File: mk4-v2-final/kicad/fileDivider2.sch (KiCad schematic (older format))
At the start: 2 parts

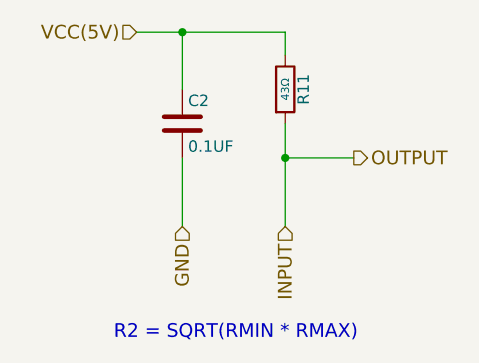
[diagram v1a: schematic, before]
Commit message: added headnight diodes, I don't think software control of them is going to be possible
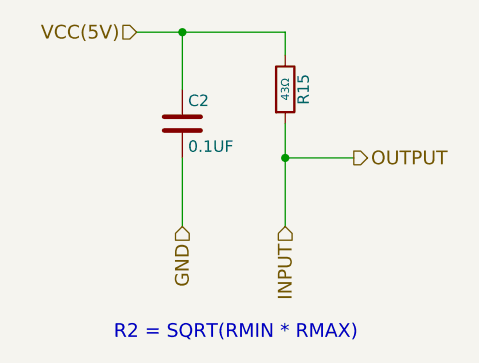
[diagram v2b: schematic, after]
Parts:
- renumbered R11 to R15
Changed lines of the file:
@@
 $EndDescr
 $Comp
-L R R11
+L R R15
 U 1 1 59DE51A6
 P 5850 3200
-F 0 "R11" V 5930 3200 50  0000 C CNN
+F 0 "R15" V 5930 3200 50  0000 C CNN
 F 1 "43Ω" V 5850 3200 35  0000 C CNN
 F 2 "Resistors_THT:R_Axial_DIN0207_L6.3mm_D2.5mm_P10.16mm_Horizontal" V 5780 3200 50  0001 C CNN

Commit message: schematic is done, footprint association and netlist are also done
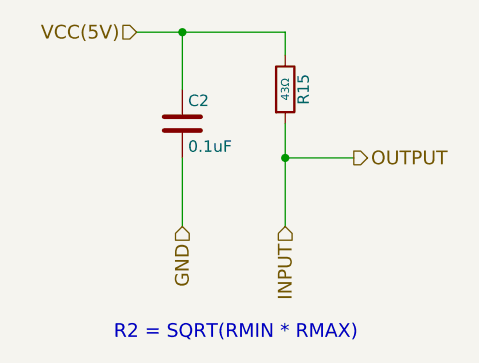
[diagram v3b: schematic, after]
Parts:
- C2: value 0.1UF -> 0.1uF; footprint Capacitors_THT:CP_Radial_D5.0mm_P2.00mm -> C_Rect_L5.08mm_W3.175mm_P2.54mm:C_Rect_L5.08mm_W3.175mm_P2.54mm; digikey-pn (none) -> 478-5096-ND; mfg-pn (none) -> AR205F104K4R
- R15: footprint Resistors_THT:R_Axial_DIN0207_L6.3mm_D2.5mm_P10.16mm_Horizontal -> Resistors_THT:R_Axial_DIN0204_L3.6mm_D1.6mm_P5.08mm_Horizontal; digikey-pn (none) -> BC4443CT-ND; mfg-pn (none) -> MBA02040C4309FC100
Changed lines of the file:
@@
 EESchema Schematic File Version 2
-LIBS:hitchco-mk4-rescue
 LIBS:power
 LIBS:device
@@
 LIBS:cd4013b
 LIBS:ncs3s1205sc
+LIBS:lca715
+LIBS:SN74HC595N
+LIBS:CD74HC4067
 LIBS:hitchco-mk4-cache
 EELAYER 25 0
@@
 F 0 "R15" V 5930 3200 50  0000 C CNN
 F 1 "43Ω" V 5850 3200 35  0000 C CNN
-F 2 "Resistors_THT:R_Axial_DIN0207_L6.3mm_D2.5mm_P10.16mm_Horizontal" V 5780 3200 50  0001 C CNN
+F 2 "Resistors_THT:R_Axial_DIN0204_L3.6mm_D1.6mm_P5.08mm_Horizontal" V 5780 3200 50  0001 C CNN
 F 3 "" H 5850 3200 50  0001 C CNN
+F 4 "BC4443CT-ND" H 5930 3300 50  0001 C CNN "digikey-pn"
+F 5 "MBA02040C4309FC100" H 5930 3300 50  0001 C CNN "mfg-pn"
 	1    5850 3200
+	1    0    0    -1
+$EndComp
+$Comp
+L C C2
+U 1 1 5A23F9FC
+P 5400 3350
+F 0 "C2" H 5425 3450 50  0000 L CNN
+F 1 "0.1uF" H 5425 3250 50  0000 L CNN
+F 2 "C_Rect_L5.08mm_W3.175mm_P2.54mm:C_Rect_L5.08mm_W3.175mm_P2.54mm" H 5438 3200 50  0001 C CNN
+F 3 "http://datasheets.avx.com/AR-Series.pdf" H 5400 3350 50  0001 C CNN
+F 4 "478-5096-ND" H 5425 3550 50  0001 C CNN "digikey-pn"
+F 5 "AR205F104K4R" H 5425 3550 50  0001 C CNN "mfg-pn"
+	1    5400 3350
 	1    0    0    -1
 $EndComp
 Text Notes 5100 4300 0    60   ~ 0
 R2 = SQRT(RMIN * RMAX)\n
-Wire Wire Line
-	5400 3500 5400 3800
-Wire Wire Line
-	5200 2950 5850 2950
-Wire Wire Line
-	5400 2950 5400 3200
-Connection ~ 5400 2950
-Wire Wire Line
-	5850 3500 6150 3500
-Connection ~ 5850 3500
 Text HLabel 5850 3800 3    60   Input ~ 0
 INPUT
-Wire Wire Line
-	5850 3350 5850 3800
 Text HLabel 6150 3500 2    60   Output ~ 0
 OUTPUT
@@
 VCC(5V)
 Wire Wire Line
+	5400 3500 5400 3800
+Wire Wire Line
+	5200 2950 5850 2950
+Wire Wire Line
+	5400 2950 5400 3200
+Wire Wire Line
+	5850 3500 6150 3500
+Wire Wire Line
+	5850 3350 5850 3800
+Wire Wire Line
 	5850 2950 5850 3050
-$Comp
-L C C2
-U 1 1 5A23F9FC
-P 5400 3350
-F 0 "C2" H 5425 3450 50  0000 L CNN
-F 1 "0.1UF" H 5425 3250 50  0000 L CNN
-F 2 "Capacitors_THT:CP_Radial_D5.0mm_P2.00mm" H 5438 3200 50  0001 C CNN
-F 3 "http://nichicon-us.com/english/products/pdfs/e-uvr.pdf" H 5400 3350 50  0001 C CNN
-	1    5400 3350
-	1    0    0    -1
-$EndComp
+Connection ~ 5400 2950
+Connection ~ 5850 3500
 $EndSCHEMATC
